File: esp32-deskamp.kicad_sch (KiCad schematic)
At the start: 29 parts, among them J1 INPUT 00, J10 ADDITIONAL GPIO, J2 INPUT 01, J3 MUTE, J4 SLEEP, J5 PRE OUT, J6 LFE OUT, J7 INPUT SELECT, J8 MOTOR, J9 12V IN, K1 INPUT 00, K2 INPUT 01, K3 AMP MUTE, K4 AMP SLEEP, U1 ESP32 D1 MINI, U2 TSR 1-2433, U3 L9110, U4 ULN2003A

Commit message: Fix cap footprint, moar layout
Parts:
- C1: footprint Capacitor_THT:DX_5R5VxxxxU_D11.5mm_P5.00mm -> Capacitor_THT:CP_Radial_D5.0mm_P2.00mm
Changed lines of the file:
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@@
 			)
 		)
-		(property "Footprint" "Capacitor_THT:DX_5R5VxxxxU_D11.5mm_P5.00mm"
+		(property "Footprint" "Capacitor_THT:CP_Radial_D5.0mm_P2.00mm"
 			(at 134.3152 120.65 0)
 			(effects

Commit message: IC routing
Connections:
- net Input1: now also U1.31 (IO_16/D4); no longer U1.25 (IO_22/D1/SCL)
- net Mute: now also U1.25 (IO_22/D1/SCL); no longer U1.31 (IO_16/D4)

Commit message: IC routing
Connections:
- net Input0: now also U4.7 (I7); no longer U4.6 (I6)
- net Input1: now also U4.6 (I6); no longer U4.7 (I7)
- net Mute: now also U4.5 (I5); no longer U4.4 (I4)
- net PWM0: now also U3.6 (IA); no longer U3.7 (IB)
- net PWM1: now also U3.7 (IB); no longer U3.6 (IA)
- net Relay0: now also U4.10 (O7); no longer U4.11 (O6)
- net Relay1: now also U4.11 (O6); no longer U4.10 (O7)
- net Relay2: now also U4.12 (O5); no longer U4.13 (O4)
- net Relay3: now also U4.13 (O4); no longer U4.12 (O5)
- net Sleep: now also U4.4 (I4); no longer U4.5 (I5)
- no-connect marks 30 -> 51

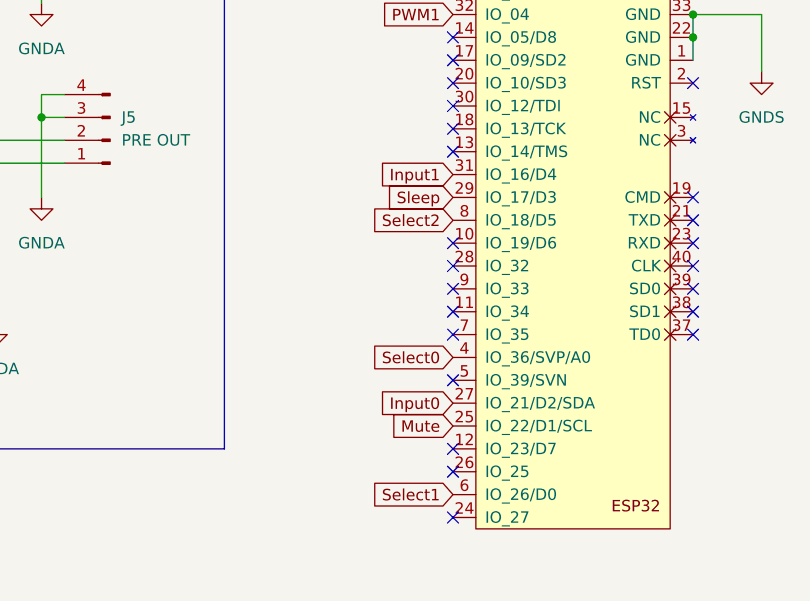
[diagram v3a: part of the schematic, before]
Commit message: Finish routing, start DRC
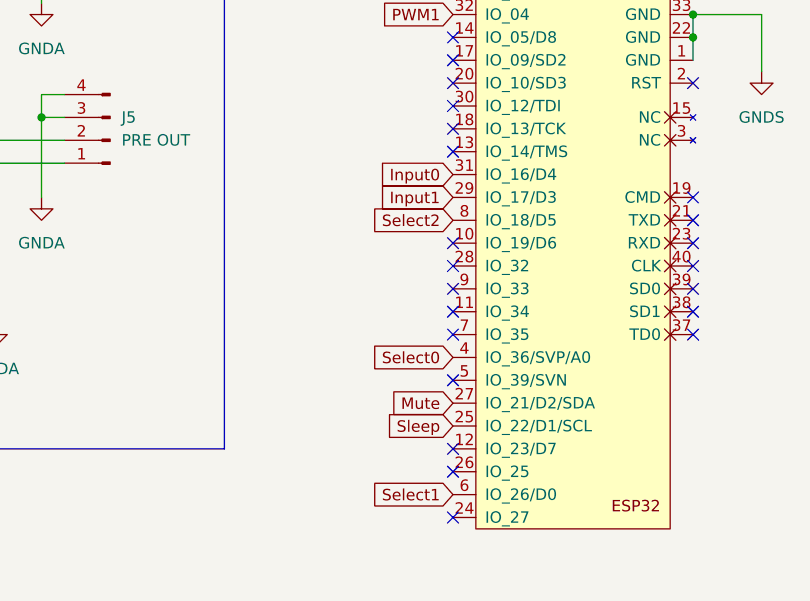
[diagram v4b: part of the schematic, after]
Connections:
- net Input0: now also U1.31 (IO_16/D4); no longer U1.27 (IO_21/D2/SDA)
- net Input1: now also U1.29 (IO_17/D3); no longer U1.31 (IO_16/D4)
- net Mute: now also U1.27 (IO_21/D2/SDA); no longer U1.25 (IO_22/D1/SCL)
- net Sleep: now also U1.25 (IO_22/D1/SCL); no longer U1.29 (IO_17/D3)

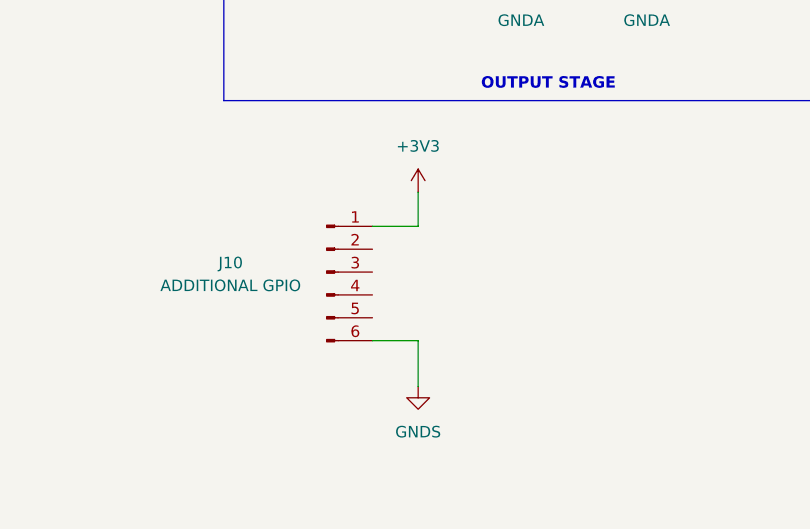
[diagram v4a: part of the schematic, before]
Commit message: Name nets
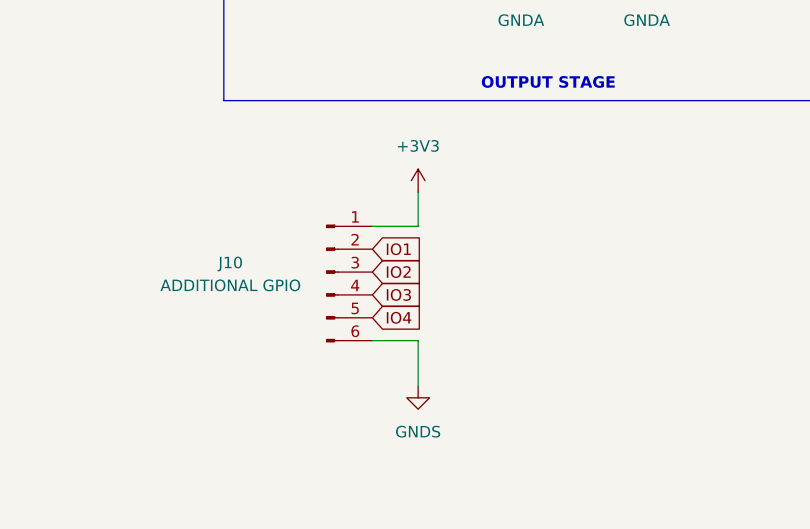
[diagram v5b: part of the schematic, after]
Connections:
- net IO1: now reaches J10.2 (Pin_2)
- net IO2: now reaches J10.3 (Pin_3)
- net IO3: now reaches J10.4 (Pin_4)
- net IO4: now reaches J10.5 (Pin_5)
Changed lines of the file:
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@@
+		)
+	)
+	(global_label "IO3"
+		(shape input)
+		(at 160.02 167.64 0)
+		(fields_autoplaced yes)
+		(effects
+			(font
+				(size 1.27 1.27)
+			)
+			(justify left)
+		)
+		(property "Intersheetrefs" "${INTERSHEET_REFS}"
+			(at 166.15 167.64 0)
+			(effects
+				(font
+					(size 1.27 1.27)
+				)
+				(justify left)
+				(hide yes)
+			)
+		)
+	)
+	(global_label "IO1"
+		(shape input)
+		(at 160.02 162.56 0)
+		(fields_autoplaced yes)
+		(effects
+			(font
+				(size 1.27 1.27)
+			)
+			(justify left)
+		)
+		(property "Intersheetrefs" "${INTERSHEET_REFS}"
+			(at 166.15 162.56 0)
+			(effects
+				(font
+					(size 1.27 1.27)
+				)
+				(justify left)
+				(hide yes)
+			)
 		)
 	)
@@
 		)
 	)
+	(global_label "IO4"
+		(shape input)
+		(at 160.02 170.18 0)
+		(fields_autoplaced yes)
+		(effects
+			(font
+				(size 1.27 1.27)
+			)
+			(justify left)
+		)
+		(property "Intersheetrefs" "${INTERSHEET_REFS}"
+			(at 166.15 170.18 0)
+			(effects
+				(font
+					(size 1.27 1.27)
+				)
+				(justify left)
+				(hide yes)
+			)
+		)
+	)
 	(global_label "Select0"
 		(shape input)
@@
 			(effects
 				(font
+					(size 1.27 1.27)
+				)
+				(justify left)
+				(hide yes)
+			)
+		)
+	)
+	(global_label "IO2"
+		(shape input)
+		(at 160.02 165.1 0)
+		(fields_autoplaced yes)
+		(effects
+			(font
+				(size 1.27 1.27)
+			)
+			(justify left)
+		)
+		(property "Intersheetrefs" "${INTERSHEET_REFS}"
+			(at 166.15 165.1 0)
+			(effects
+				(font

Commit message: Move cap
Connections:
- net +3V3: now also J10.5 (Pin_5); no longer J10.1 (Pin_1)
- net IO1: now also J10.1 (Pin_1); no longer J10.2 (Pin_2)
- net IO2: now also J10.2 (Pin_2); no longer J10.3 (Pin_3)
- net IO3: now also J10.3 (Pin_3); no longer J10.4 (Pin_4)
- net IO4: now also J10.4 (Pin_4); no longer J10.5 (Pin_5)
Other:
- moved on the sheet: J10
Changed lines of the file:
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@@
 	(wire
 		(pts
+			(xy 148.59 173.99) (xy 156.21 173.99)
+		)
+		(stroke
+			(width 0)
+			(type default)
+		)
+	)
+	(wire
+		(pts
 			(xy 46.99 31.75) (xy 46.99 41.91)
 		)
@@
 	(wire
 		(pts
-			(xy 165.1 172.72) (xy 165.1 177.8)
+			(xy 156.21 176.53) (xy 156.21 181.61)
 		)
 		(stroke
@@
 	(wire
 		(pts
-			(xy 160.02 160.02) (xy 165.1 160.02)
+			(xy 156.21 160.02) (xy 156.21 173.99)
 		)
 		(stroke
@@
 	(wire
 		(pts
-			(xy 160.02 172.72) (xy 165.1 172.72)
+			(xy 148.59 176.53) (xy 156.21 176.53)
 		)
 		(stroke
@@
 	(wire
 		(pts
-			(xy 165.1 156.21) (xy 165.1 160.02)
-		)
-		(stroke
-			(width 0)
-			(type default)
-		)
-	)
-	(wire
-		(pts
 			(xy 224.79 62.23) (xy 224.79 57.15)
 		)
@@
 	(global_label "IO3"
 		(shape input)
-		(at 160.02 167.64 0)
+		(at 148.59 168.91 0)
 		(fields_autoplaced yes)
 		(effects
@@
 		)
 		(property "Intersheetrefs" "${INTERSHEET_REFS}"
-			(at 166.15 167.64 0)
+			(at 154.72 168.91 0)
 			(effects
 				(font
@@
 	(global_label "IO1"
 		(shape input)
-		(at 160.02 162.56 0)
+		(at 148.59 163.83 0)
 		(fields_autoplaced yes)
 		(effects
@@
 		)
 		(property "Intersheetrefs" "${INTERSHEET_REFS}"
-			(at 166.15 162.56 0)
+			(at 154.72 163.83 0)
 			(effects
 				(font
@@
 	(global_label "IO4"
 		(shape input)
-		(at 160.02 170.18 0)
+		(at 148.59 171.45 0)
 		(fields_autoplaced yes)
 		(effects
@@
 		)
 		(property "Intersheetrefs" "${INTERSHEET_REFS}"
-			(at 166.15 170.18 0)
+			(at 154.72 171.45 0)
 			(effects
 				(font
@@
 	(global_label "IO2"
 		(shape input)
-		(at 160.02 165.1 0)
+		(at 148.59 166.37 0)
 		(fields_autoplaced yes)
 		(effects
@@
 		)
 		(property "Intersheetrefs" "${INTERSHEET_REFS}"
-			(at 166.15 165.1 0)
+			(at 154.72 166.37 0)
 			(effects
 				(font
@@
 	(symbol
 		(lib_id "power:+3V3")
-		(at 165.1 156.21 0)
+		(at 156.21 160.02 0)
 		(unit 1)
 		(exclude_from_sim no)
@@
 		(fields_autoplaced yes)
 		(property "Reference" "#PWR027"
-			(at 165.1 160.02 0)
+			(at 156.21 163.83 0)
 			(effects
 				(font
@@
 		)
 		(property "Value" "+3V3"
-			(at 165.1 151.13 0)
+			(at 156.21 154.94 0)
 			(effects
 				(font
@@
 		)
 		(property "Footprint" ""
-			(at 165.1 156.21 0)
+			(at 156.21 160.02 0)
 			(effects
 				(font
@@
 		)
 		(property "Datasheet" ""
-			(at 165.1 156.21 0)
+			(at 156.21 160.02 0)
 			(effects
 				(font
@@
 		)
 		(property "Description" "Power symbol creates a global label with name \"+3V3\""
-			(at 165.1 156.21 0)
+			(at 156.21 160.02 0)
 			(effects
 				(font
@@
 	(symbol
 		(lib_id "power:GNDS")
-		(at 165.1 177.8 0)
+		(at 156.21 181.61 0)
 		(unit 1)
 		(exclude_from_sim no)
@@
 		(fields_autoplaced yes)
 		(property "Reference" "#PWR028"
-			(at 165.1 184.15 0)
+			(at 156.21 187.96 0)
 			(effects
 				(font
@@
 		)
 		(property "Value" "GNDS"
-			(at 165.1 182.88 0)
+			(at 156.21 186.69 0)
 			(effects
 				(font
@@
 		)
 		(property "Footprint" ""
-			(at 165.1 177.8 0)
+			(at 156.21 181.61 0)
 			(effects
 				(font
@@
 		)
 		(property "Datasheet" ""
-			(at 165.1 177.8 0)
+			(at 156.21 181.61 0)
 			(effects
 				(font
@@
 		)
 		(property "Description" "Power symbol creates a global label with name \"GNDS\" , signal ground"
-			(at 165.1 177.8 0)
+			(at 156.21 181.61 0)
 			(effects
 				(font
@@
 	(symbol
 		(lib_id "Connector:Conn_01x06_Pin")
-		(at 154.94 165.1 0)
+		(at 143.51 168.91 0)
 		(unit 1)
 		(exclude_from_sim no)
@@
 		(dnp no)
 		(property "Reference" "J10"
-			(at 144.272 164.084 0)
+			(at 132.842 167.894 0)
 			(effects
 				(font
@@
 		)
 		(property "Value" "ADDITIONAL GPIO"
-			(at 144.272 166.624 0)
+			(at 132.842 170.434 0)
 			(effects
 				(font
@@
 		)
 		(property "Footprint" "Connector_PinHeader_2.54mm:PinHeader_1x06_P2.54mm_Vertical"
-			(at 154.94 165.1 0)
+			(at 143.51 168.91 0)
 			(effects
 				(font
@@
 		)
 		(property "Datasheet" "~"
-			(at 154.94 165.1 0)
+			(at 143.51 168.91 0)
 			(effects
 				(font
@@
 		)
 		(property "Description" "Generic connector, single row, 01x06, script generated"
-			(at 154.94 165.1 0)
+			(at 143.51 168.91 0)
 			(effects
 				(font

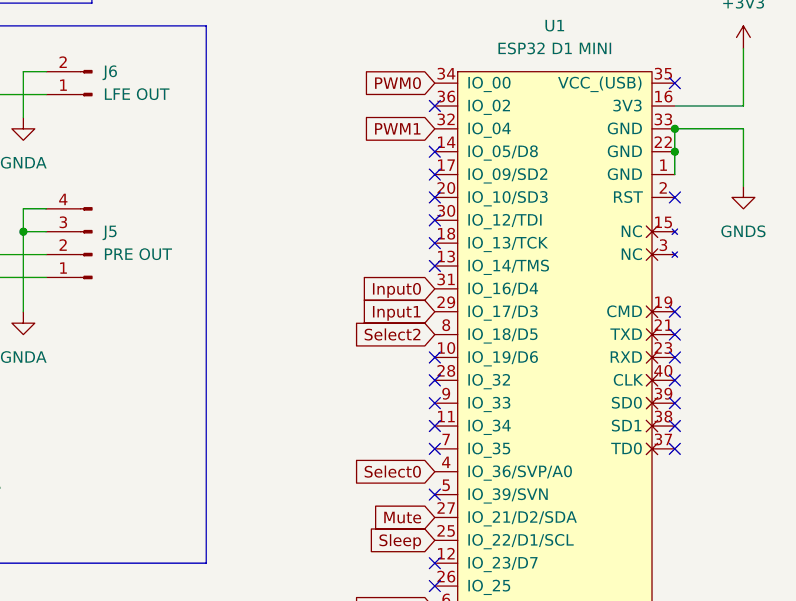
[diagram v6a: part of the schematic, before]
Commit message: Resolve DRC warnings
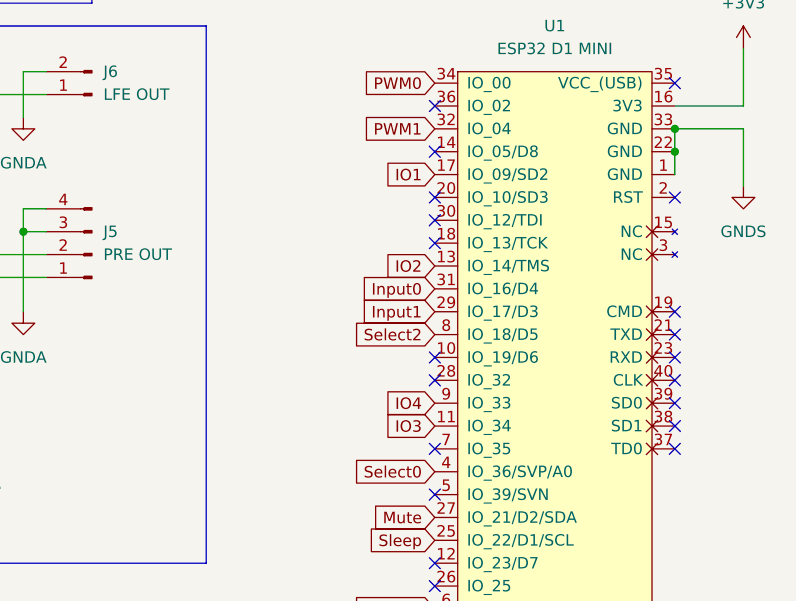
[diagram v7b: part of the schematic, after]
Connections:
- net IO1: now also U1.17 (IO_09/SD2)
- net IO2: now also U1.13 (IO_14/TMS)
- net IO3: now also U1.11 (IO_34)
- net IO4: now also U1.9 (IO_33)
- no-connect marks 51 -> 47
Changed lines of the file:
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@@
-	)
-	(no_connect
-		(at 241.3 102.87)
 	)
 	(no_connect
@@
 	)
 	(no_connect
-		(at 241.3 130.81)
-	)
-	(no_connect
 		(at 77.47 81.28)
 	)
@@
 	)
 	(no_connect
-		(at 241.3 113.03)
-	)
-	(no_connect
 		(at 241.3 110.49)
 	)
@@
 	)
 	(no_connect
-		(at 241.3 128.27)
-	)
-	(no_connect
 		(at 77.47 44.45)
 	)
@@
 		)
 	)
+	(global_label "IO2"
+		(shape input)
+		(at 241.3 113.03 180)
+		(fields_autoplaced yes)
+		(effects
+			(font
+				(size 1.27 1.27)
+			)
+			(justify right)
+		)
+		(property "Intersheetrefs" "${INTERSHEET_REFS}"
+			(at 235.17 113.03 0)
+			(effects
+				(font
+					(size 1.27 1.27)
+				)
+				(justify right)
+				(hide yes)
+			)
+		)
+	)
 	(global_label "Input0"
 		(shape input)
@@
 		)
 	)
+	(global_label "IO3"
+		(shape input)
+		(at 241.3 130.81 180)
+		(fields_autoplaced yes)
+		(effects
+			(font
+				(size 1.27 1.27)
+			)
+			(justify right)
+		)
+		(property "Intersheetrefs" "${INTERSHEET_REFS}"
+			(at 235.17 130.81 0)
+			(effects
+				(font
+					(size 1.27 1.27)
+				)
+				(justify right)
+				(hide yes)
+			)
+		)
+	)
 	(global_label "PRE_RIGHT"
 		(shape input)
@@
 		)
 	)
+	(global_label "IO1"
+		(shape input)
+		(at 241.3 102.87 180)
+		(fields_autoplaced yes)
+		(effects
+			(font
+				(size 1.27 1.27)
+			)
+			(justify right)
+		)
+		(property "Intersheetrefs" "${INTERSHEET_REFS}"
+			(at 235.17 102.87 0)
+			(effects
+				(font
+					(size 1.27 1.27)
+				)
+				(justify right)
+				(hide yes)
+			)
+		)
+	)
 	(global_label "Relay2"
 		(shape input)
@@
 				(hide yes)
 			)
+		)
+	)
+	(global_label "IO4"
+		(shape input)
+		(at 241.3 128.27 180)
+		(fields_autoplaced yes)
+		(effects
+			(font
+				(size 1.27 1.27)
+			)
+			(justify right)
+		)
+		(property "Intersheetrefs" "${INTERSHEET_REFS}"
+			(at 235.17 128.27 0)
+			(effects
+				(font
+					(size 1.27 1.27)
+				)
+				(justify right)
+				(hide yes)
+			)

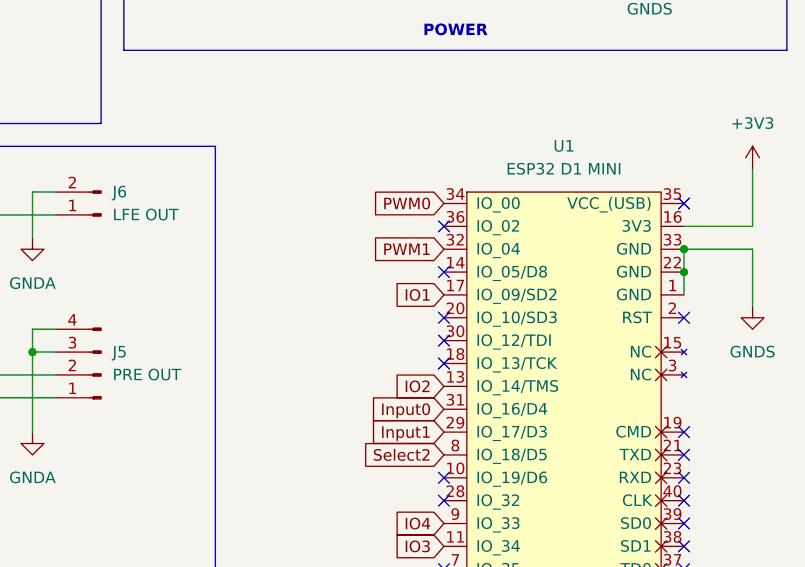
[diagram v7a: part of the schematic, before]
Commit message: Fix edge cuts
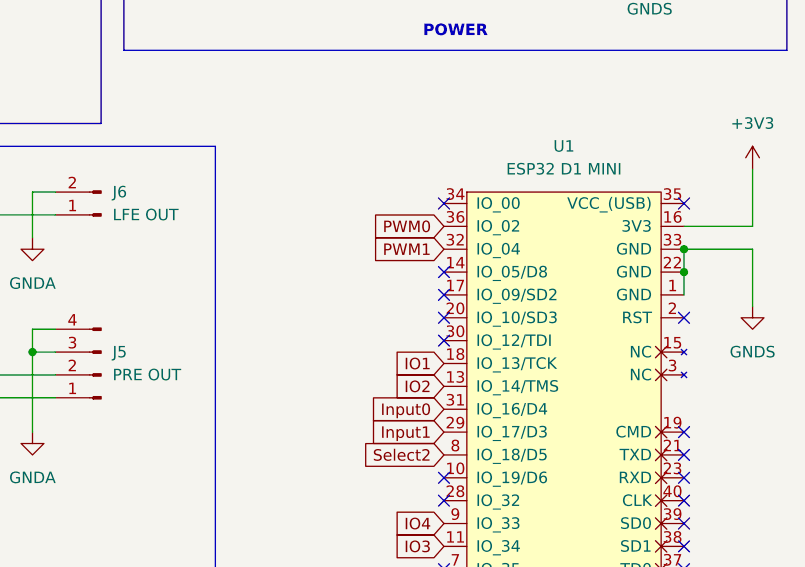
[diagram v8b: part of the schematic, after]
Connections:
- net IO1: now also U1.18 (IO_13/TCK); no longer U1.17 (IO_09/SD2)
- net PWM0: now also U1.36 (IO_02); no longer U1.34 (IO_00)
